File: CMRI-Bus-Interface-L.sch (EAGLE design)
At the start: 19 parts, among them CON1 0.100, CON2 0.100, U1 MAX3465CPD, U2 NE555

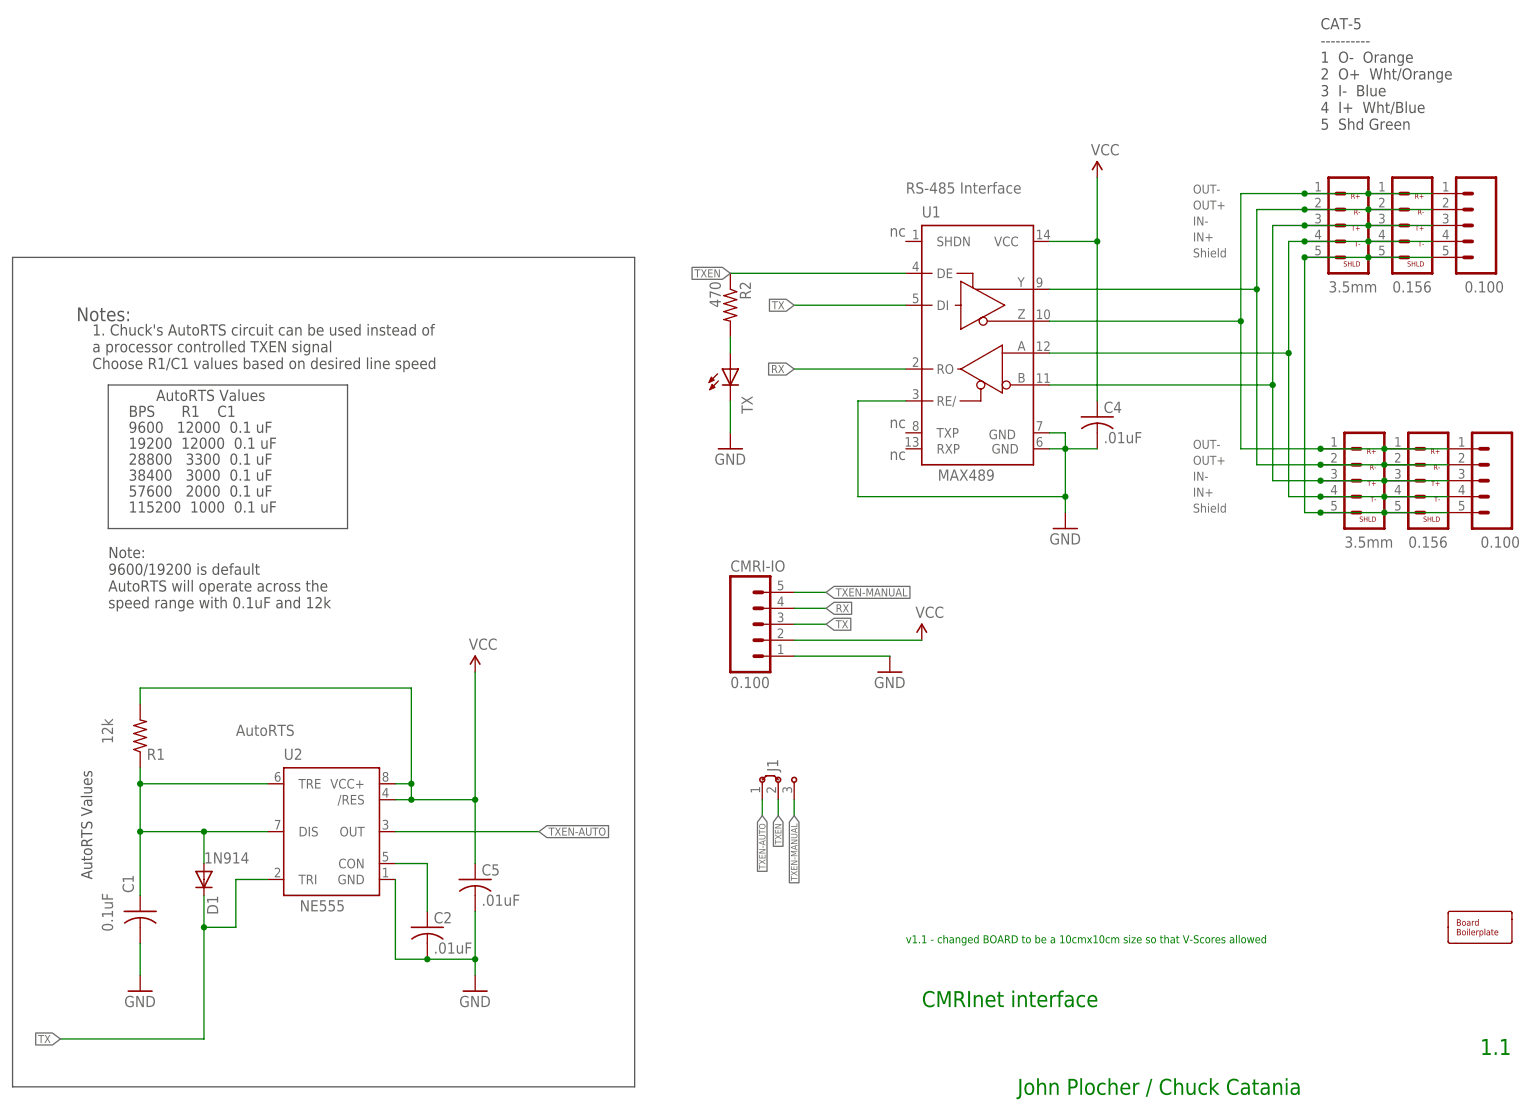
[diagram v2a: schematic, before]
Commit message: SMT cost reduce
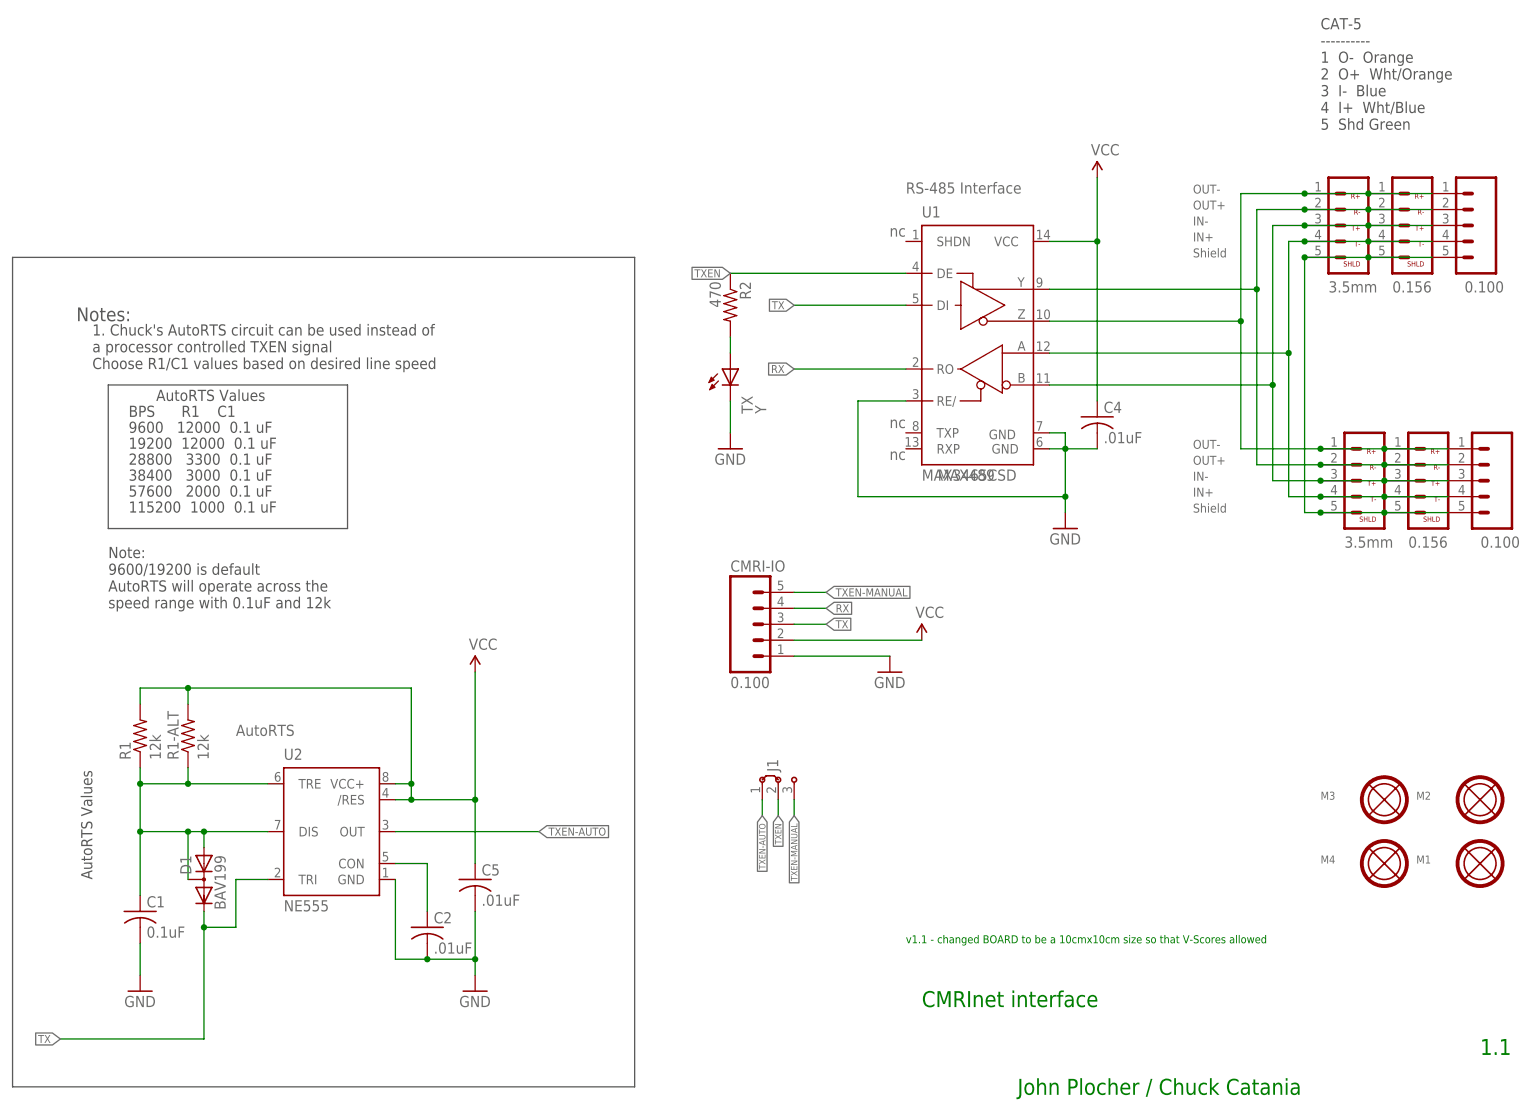
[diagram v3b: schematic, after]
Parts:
- removed BOARD1: BOARD80X60, SPCoast:BOARD80X60
- added M1, M2, M3, M4: MOUNTINGHOLE, SPCoast:MOUNTINGHOLE
- added R1-ALT: 12k, SPCoast:R0805-RES
- C1, C2: device SPCoast:CAPPTH1 -> SPCoast:CAP0603
- C4, C5: device SPCoast:CAPPTH2 -> SPCoast:CAP0603
- D1: value 1N4148 -> BAV199; device SPCoast:DIODE1N4148 -> SPCoast:DIODE-BAV199
- R1: device SPCoast:RPTH03 -> SPCoast:RPTH04
- R2: device SPCoast:RPTH03 -> SPCoast:R0805-RES
- TX: value (none) -> Y; device SPCoast:LEDLED5MM -> SPCoast:LED0603-LED
- U1: value MAX3465CPD -> MAX3465CSD; device SPCoast:MAX3465CPD -> SPCoast:MAX3465CSD
- U2: device SPCoast:NE555P -> SPCoast:NE555D
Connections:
- net N$52: now also D1.AC, R1-ALT.1
- net VCC: now also R1-ALT.2
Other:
- note removed: "1N914"

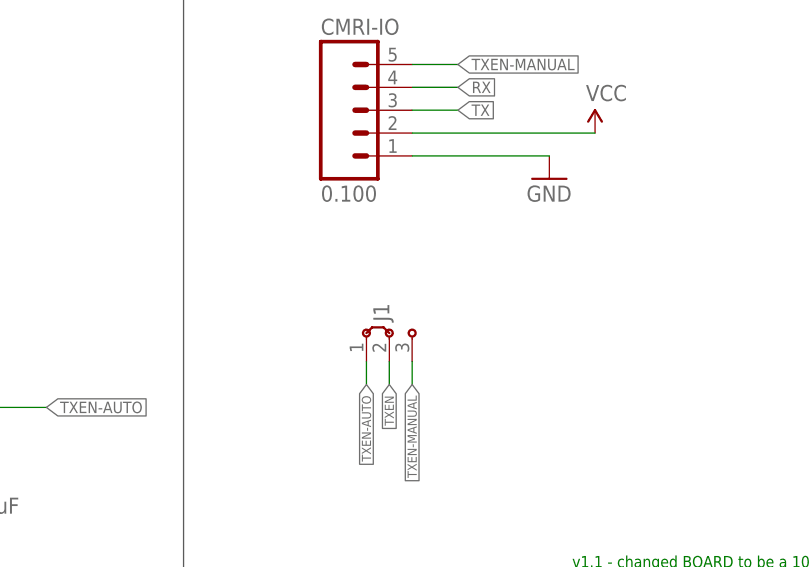
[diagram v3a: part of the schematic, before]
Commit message: added values for connectors
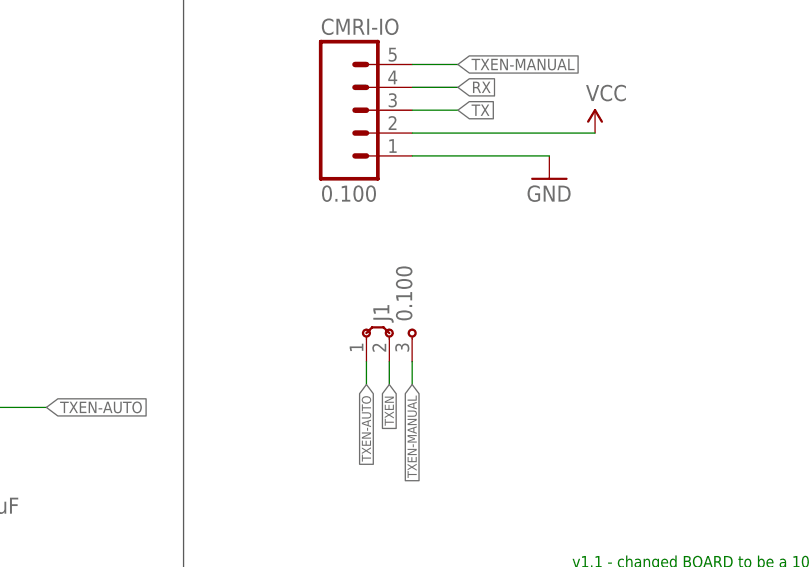
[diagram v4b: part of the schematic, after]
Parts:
- J1: value (none) -> 0.100
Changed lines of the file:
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@@
 <grid distance="100" unitdist="mil" unit="mil" style="dots" multiple="1" display="yes" altdistance="50" altunitdist="mil" altunit="mil"/>
 <layers>
-<layer number="1" name="Top" color="4" fill="1" visible="yes" active="no"/>
-<layer number="2" name="Route2" color="1" fill="3" visible="yes" active="no"/>
-<layer number="3" name="Route3" color="4" fill="3" visible="yes" active="no"/>
-<layer number="14" name="Route14" color="1" fill="6" visible="yes" active="no"/>
-<layer number="15" name="Route15" color="4" fill="6" visible="yes" active="no"/>
-<layer number="16" name="Bottom" color="2" fill="1" visible="yes" active="no"/>
-<layer number="17" name="Pads" color="23" fill="1" visible="yes" active="no"/>
-<layer number="18" name="Vias" color="29" fill="1" visible="yes" active="no"/>
-<layer number="19" name="Unrouted" color="6" fill="1" visible="yes" active="no"/>
-<layer number="20" name="Dimension" color="15" fill="1" visible="yes" active="no"/>
-<layer number="21" name="tPlace" color="19" fill="1" visible="yes" active="no"/>
-<layer number="22" name="bPlace" color="17" fill="1" visible="yes" active="no"/>
-<layer number="23" name="tOrigins" color="30" fill="1" visible="yes" active="no"/>
-<layer number="24" name="bOrigins" color="15" fill="1" visible="yes" active="no"/>
-<layer number="25" name="tNames" color="63" fill="1" visible="yes" active="no"/>
-<layer number="26" name="bNames" color="34" fill="1" visible="yes" active="no"/>
-<layer number="27" name="tValues" color="56" fill="1" visible="yes" active="no"/>
-<layer number="28" name="bValues" color="7" fill="1" visible="yes" active="no"/>
+<layer number="1" name="Top" color="4" fill="1" visible="no" active="no"/>
+<layer number="2" name="Route2" color="1" fill="3" visible="no" active="no"/>
+<layer number="3" name="Route3" color="4" fill="3" visible="no" active="no"/>
+<layer number="14" name="Route14" color="1" fill="6" visible="no" active="no"/>
+<layer number="15" name="Route15" color="4" fill="6" visible="no" active="no"/>
+<layer number="16" name="Bottom" color="2" fill="1" visible="no" active="no"/>
+<layer number="17" name="Pads" color="23" fill="1" visible="no" active="no"/>
+<layer number="18" name="Vias" color="29" fill="1" visible="no" active="no"/>
+<layer number="19" name="Unrouted" color="6" fill="1" visible="no" active="no"/>
+<layer number="20" name="Dimension" color="15" fill="1" visible="no" active="no"/>
+<layer number="21" name="tPlace" color="19" fill="1" visible="no" active="no"/>
+<layer number="22" name="bPlace" color="17" fill="1" visible="no" active="no"/>
+<layer number="23" name="tOrigins" color="30" fill="1" visible="no" active="no"/>
+<layer number="24" name="bOrigins" color="15" fill="1" visible="no" active="no"/>
+<layer number="25" name="tNames" color="63" fill="1" visible="no" active="no"/>
+<layer number="26" name="bNames" color="34" fill="1" visible="no" active="no"/>
+<layer number="27" name="tValues" color="56" fill="1" visible="no" active="no"/>
+<layer number="28" name="bValues" color="7" fill="1" visible="no" active="no"/>
 <layer number="29" name="tStop" color="7" fill="3" visible="no" active="no"/>
 <layer number="30" name="bStop" color="7" fill="6" visible="no" active="no"/>
@@
 <layer number="35" name="tGlue" color="7" fill="4" visible="no" active="no"/>
 <layer number="36" name="bGlue" color="7" fill="5" visible="no" active="no"/>
-<layer number="37" name="tTest" color="7" fill="1" visible="yes" active="no"/>
-<layer number="38" name="bTest" color="7" fill="1" visible="yes" active="no"/>
+<layer number="37" name="tTest" color="7" fill="1" visible="no" active="no"/>
+<layer number="38" name="bTest" color="7" fill="1" visible="no" active="no"/>
 <layer number="39" name="tKeepout" color="4" fill="11" visible="no" active="no"/>
 <layer number="40" name="bKeepout" color="3" fill="11" visible="no" active="no"/>
@@
 <layer number="44" name="Drills" color="16" fill="1" visible="no" active="no"/>
 <layer number="45" name="Holes" color="35" fill="1" visible="no" active="no"/>
-<layer number="46" name="Milling" color="35" fill="1" visible="yes" active="no"/>
-<layer number="47" name="Measures" color="21" fill="1" visible="yes" active="no"/>
-<layer number="48" name="Document" color="47" fill="1" visible="yes" active="no"/>
-<layer number="49" name="Reference" color="48" fill="1" visible="yes" active="no"/>
-<layer number="50" name="dxf" color="7" fill="1" visible="yes" active="no"/>
-<layer number="51" name="tDocu" color="24" fill="1" visible="yes" active="no"/>
-<layer number="52" name="bDocu" color="7" fill="1" visible="yes" active="no"/>
-<layer number="53" name="tGND_GNDA" color="7" fill="9" visible="yes" active="no"/>
-<layer number="54" name="bGND_GNDA" color="1" fill="9" visible="yes" active="no"/>
-<layer number="56" name="wert" color="7" fill="1" visible="yes" active="no"/>
-<layer number="57" name="tCAD" color="7" fill="1" visible="yes" active="no"/>
-<layer number="59" name="tCarbon" color="7" fill="1" visible="yes" active="no"/>
-<layer number="60" name="bCarbon" color="7" fill="1" visible="yes" active="no"/>
+<layer number="46" name="Milling" color="35" fill="1" visible="no" active="no"/>
+<layer number="47" name="Measures" color="21" fill="1" visible="no" active="no"/>
+<layer number="48" name="Document" color="47" fill="1" visible="no" active="no"/>
+<layer number="49" name="Reference" color="48" fill="1" visible="no" active="no"/>
+<layer number="50" name="dxf" color="7" fill="1" visible="no" active="no"/>
+<layer number="51" name="tDocu" color="24" fill="1" visible="no" active="no"/>
+<layer number="52" name="bDocu" color="7" fill="1" visible="no" active="no"/>
+<layer number="53" name="tGND_GNDA" color="7" fill="9" visible="no" active="no"/>
+<layer number="54" name="bGND_GNDA" color="1" fill="9" visible="no" active="no"/>
+<layer number="56" name="wert" color="7" fill="1" visible="no" active="no"/>
+<layer number="57" name="tCAD" color="7" fill="1" visible="no" active="no"/>
+<layer number="59" name="tCarbon" color="7" fill="1" visible="no" active="no"/>
+<layer number="60" name="bCarbon" color="7" fill="1" visible="no" active="no"/>
 <layer number="90" name="Modules" color="5" fill="1" visible="yes" active="yes"/>
 <layer number="91" name="Nets" color="2" fill="1" visible="yes" active="yes"/>
@@
 <part name="FRAME1" library="SPCoast" deviceset="DOC-FRAME-LETTER" device=""/>
 <part name="GND4" library="SparkFun" deviceset="GND" device=""/>
-<part name="J1" library="SPCoast" deviceset="JUMPER-3-DEFAULT" device="2.54MM"/>
+<part name="J1" library="SPCoast" deviceset="JUMPER-3-DEFAULT" device="2.54MM" value="0.100"/>
 <part name="CON1" library="SPCoast" deviceset="CONNECTOR-M05" device="LOCK" value="0.100"/>
 <part name="CON2" library="SPCoast" deviceset="CONNECTOR-M05" device="LOCK" value="0.100"/>
